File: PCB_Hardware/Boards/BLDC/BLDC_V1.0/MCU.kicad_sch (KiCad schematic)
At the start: 15 parts, among them J7 Conn_ARM_JTAG_SWD_10, U7 STM32G474RET6, Y2 XXGBBCNANF-25.000000MHZ

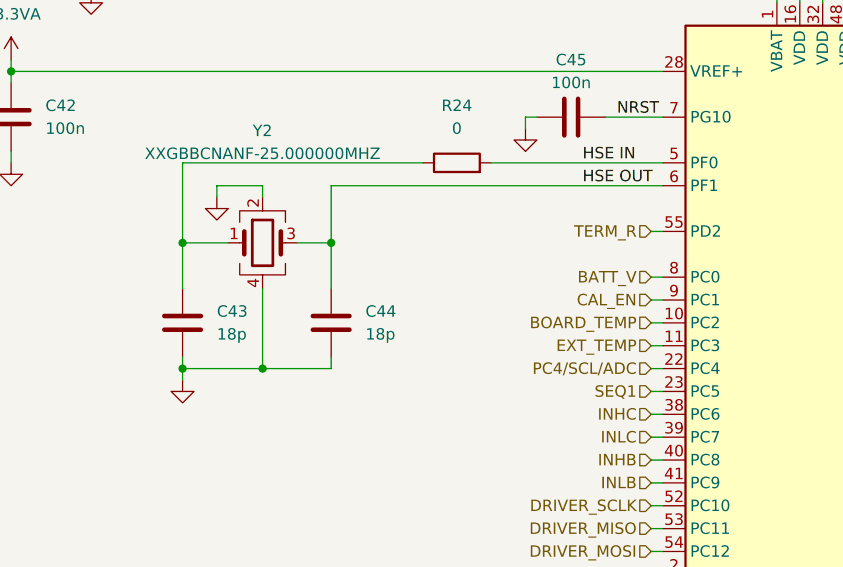
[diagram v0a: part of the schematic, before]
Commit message: Add DBcan transport refactor, BLDC V1.0 schematic + sim work, HAL submodule
- DBcan: replace bare-register driver with vendor-agnostic transport abstraction (core/, transports/, refactored bootloader driver, README)
- Add stm32g4xx_hal_driver as Firmware/libs submodule
- Add HAL config for BLDC board (stm32g4xx_hal_conf.h)
- BLDC V1.0: schematic edits across 10 sheets (footprint assignments, repositioning); design-doc README (gate-driver constraints, FET selection / TPH3R70APL, thermal analysis)
- ngspice simulation workflow (cap sweeps, half-bridge slow turn-on)
- Ignore .obsidian/ vault state and large simulation CSV exports
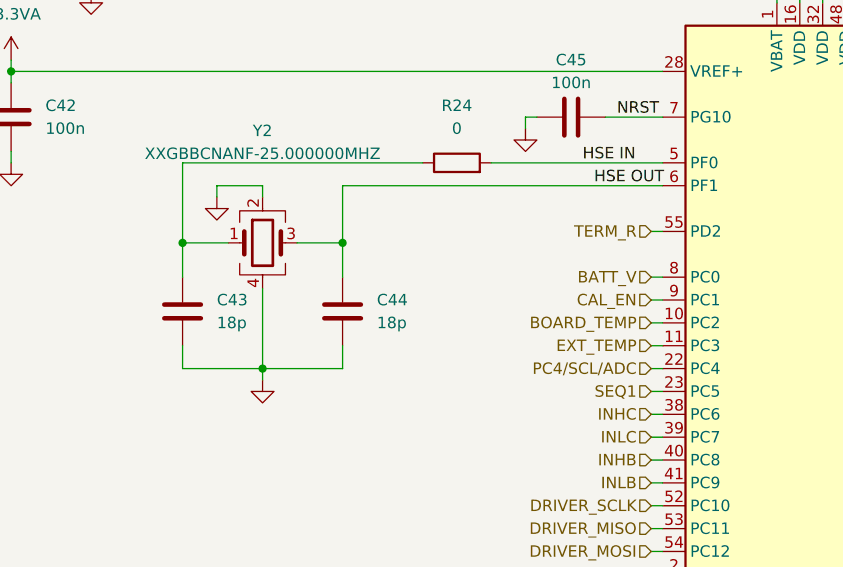
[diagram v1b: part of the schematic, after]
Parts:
- C30: footprint (none) -> Capacitor_SMD:C_0603_1608Metric
- C31, C32, C33, C34, C35, C36, C42, C45: footprint (none) -> Capacitor_SMD:C_0402_1005Metric
- R24: footprint (none) -> Resistor_SMD:R_0402_1005Metric
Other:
- moved on the sheet: C43, C44
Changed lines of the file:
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@@
 	)
 	(junction
-		(at 90.17 76.2)
-		(diameter 0)
-		(color 0 0 0 0)
-	)
-	(junction
 		(at 139.7 36.83)
 		(diameter 0)
@@
 	)
 	(junction
-		(at 73.66 76.2)
-		(diameter 0)
-		(color 0 0 0 0)
-	)
-	(junction
 		(at 88.9 46.99)
 		(diameter 0)
@@
 	)
 	(junction
-		(at 101.6 36.83)
+		(at 73.66 76.2)
 		(diameter 0)
 		(color 0 0 0 0)
 	)
 	(junction
-		(at 73.66 90.17)
+		(at 101.6 36.83)
 		(diameter 0)
 		(color 0 0 0 0)
@@
 	)
 	(junction
+		(at 91.44 76.2)
+		(diameter 0)
+		(color 0 0 0 0)
+	)
+	(junction
 		(at 139.7 48.26)
 		(diameter 0)
@@
 	(wire
 		(pts
-			(xy 82.55 90.17) (xy 90.17 90.17)
+			(xy 82.55 90.17) (xy 91.44 90.17)
 		)
 		(stroke
@@
 	(wire
 		(pts
-			(xy 90.17 69.85) (xy 90.17 76.2)
+			(xy 91.44 69.85) (xy 91.44 76.2)
 		)
 		(stroke
@@
 	(wire
 		(pts
-			(xy 73.66 81.28) (xy 73.66 76.2)
+			(xy 73.66 80.01) (xy 73.66 76.2)
 		)
 		(stroke
@@
 	(wire
 		(pts
-			(xy 73.66 88.9) (xy 73.66 90.17)
+			(xy 73.66 87.63) (xy 73.66 90.17)
 		)
 		(stroke
@@
 	(wire
 		(pts
-			(xy 90.17 81.28) (xy 90.17 76.2)
+			(xy 91.44 80.01) (xy 91.44 76.2)
 		)
 		(stroke
@@
 	(wire
 		(pts
-			(xy 90.17 88.9) (xy 90.17 90.17)
+			(xy 91.44 87.63) (xy 91.44 90.17)
 		)
 		(stroke
@@
 	(wire
 		(pts
-			(xy 127 69.85) (xy 90.17 69.85)
+			(xy 127 69.85) (xy 91.44 69.85)
 		)
 		(stroke
@@
 	(wire
 		(pts
-			(xy 73.66 90.17) (xy 73.66 91.44)
+			(xy 82.55 90.17) (xy 82.55 91.44)
 		)
 		(stroke
@@
 	(wire
 		(pts
-			(xy 86.36 76.2) (xy 90.17 76.2)
+			(xy 86.36 76.2) (xy 91.44 76.2)
 		)
 		(stroke
@@
 	)
 	(label "HSE OUT"
-		(at 118.11 69.85 0)
+		(at 119.38 69.85 0)
 		(effects
 			(font
@@
 	(symbol
 		(lib_id "Device:C")
-		(at 73.66 85.09 0)
+		(at 73.66 83.82 0)
 		(unit 1)
 		(body_style 1)
@@
 		(dnp no)
 		(property "Reference" "C43"
-			(at 77.47 83.8199 0)
+			(at 77.47 82.5499 0)
 			(show_name no)
 			(do_not_autoplace no)
@@
 		)
 		(property "Value" "18p"
-			(at 77.47 86.3599 0)
+			(at 77.47 85.0899 0)
 			(show_name no)
 			(do_not_autoplace no)
@@
 		)
 		(property "Footprint" "Capacitor_SMD:C_0402_1005Metric"
-			(at 74.6252 88.9 0)
+			(at 74.6252 87.63 0)
 			(hide yes)
 			(show_name no)
@@
 		)
 		(property "Datasheet" ""
-			(at 73.66 85.09 0)
+			(at 73.66 83.82 0)
 			(hide yes)
 			(show_name no)
@@
 		)
 		(property "Description" "Unpolarized capacitor"
-			(at 73.66 85.09 0)
+			(at 73.66 83.82 0)
 			(hide yes)
 			(show_name no)
@@
 		)
 		(property "JLCPCB Part Number" "C52923"
-			(at 73.66 85.09 0)
+			(at 73.66 83.82 0)
 			(hide yes)
 			(show_name no)
@@
 		)
 		(property "Sim.Device" ""
-			(at 73.66 85.09 0)
+			(at 73.66 83.82 0)
 			(hide yes)
 			(show_name no)
@@
 		)
 		(property "Price" ""
-			(at 73.66 85.09 0)
+			(at 73.66 83.82 0)
 			(hide yes)
 			(show_name no)
@@
 			)
 		)
-		(property "Footprint" ""
+		(property "Footprint" "Capacitor_SMD:C_0402_1005Metric"
 			(at 102.5652 45.72 0)
 			(hide yes)
@@
 	(symbol
 		(lib_id "Device:C")
-		(at 90.17 85.09 0)
+		(at 91.44 83.82 0)
 		(unit 1)
 		(body_style 1)
@@
 		(dnp no)
 		(property "Reference" "C44"
-			(at 93.98 83.8199 0)
+			(at 95.25 82.5499 0)
 			(show_name no)
 			(do_not_autoplace no)
@@
 		)
 		(property "Value" "18p"
-			(at 93.98 86.3599 0)
+			(at 95.25 85.0899 0)
 			(show_name no)
 			(do_not_autoplace no)
@@
 		)
 		(property "Footprint" "Capacitor_SMD:C_0402_1005Metric"
-			(at 91.1352 88.9 0)
+			(at 92.4052 87.63 0)
 			(hide yes)
 			(show_name no)
@@
 		)
 		(property "Datasheet" ""
-			(at 90.17 85.09 0)
+			(at 91.44 83.82 0)
 			(hide yes)
 			(show_name no)
@@
 		)
 		(property "Description" "Unpolarized capacitor"
-			(at 90.17 85.09 0)
+			(at 91.44 83.82 0)
 			(hide yes)
 			(show_name no)
@@
 		)
 		(property "JLCPCB Part Number" "C52923"
-			(at 90.17 85.09 0)
+			(at 91.44 83.82 0)
 			(hide yes)
 			(show_name no)
@@
 		)
 		(property "Sim.Device" ""
-			(at 90.17 85.09 0)
+			(at 91.44 83.82 0)
 			(hide yes)
 			(show_name no)
@@
 		)
 		(property "Price" ""
-			(at 90.17 85.09 0)
+			(at 91.44 83.82 0)
 			(hide yes)
 			(show_name no)
@@
 			)
 		)
-		(property "Footprint" ""
+		(property "Footprint" "Capacitor_SMD:C_0402_1005Metric"
 			(at 158.4452 46.99 0)
 			(hide yes)
@@
 			)
 		)
-		(property "Footprint" ""
+		(property "Footprint" "Capacitor_SMD:C_0402_1005Metric"
 			(at 89.8652 45.72 0)
 			(hide yes)
@@
 			)
 		)
-		(property "Footprint" ""
+		(property "Footprint" "Capacitor_SMD:C_0402_1005Metric"
 			(at 115.2652 45.72 0)
 			(hide yes)
@@
 	(symbol
 		(lib_id "power:GND")
-		(at 73.66 91.44 0)
+		(at 82.55 91.44 0)
 		(unit 1)
 		(body_style 1)
@@
 		(fields_autoplaced yes)
 		(property "Reference" "#PWR050"
-			(at 73.66 97.79 0)
+			(at 82.55 97.79 0)
 			(hide yes)
 			(show_name no)
@@
 		)
 		(property "Value" "GND"
-			(at 73.66 96.52 0)
+			(at 82.55 96.52 0)
 			(hide yes)
 			(show_name no)
@@
 		)
 		(property "Footprint" ""
-			(at 73.66 91.44 0)
+			(at 82.55 91.44 0)
 			(hide yes)
 			(show_name no)
@@
 		)
 		(property "Datasheet" ""
-			(at 73.66 91.44 0)
+			(at 82.55 91.44 0)
 			(hide yes)
 			(show_name no)
@@
 		)
 		(property "Description" "Power symbol creates a global label with name \"GND\" , ground"
-			(at 73.66 91.44 0)
+			(at 82.55 91.44 0)
 			(hide yes)
 			(show_name no)
@@
 			)
 		)
-		(property "Footprint" ""
+		(property "Footprint" "Capacitor_SMD:C_0402_1005Metric"
 			(at 127.9652 45.72 0)
 			(hide yes)
@@
 			)
 		)
-		(property "Footprint" ""
+		(property "Footprint" "Capacitor_SMD:C_0402_1005Metric"
 			(at 55.5752 66.04 0)
 			(hide yes)
@@
 			)
 		)
-		(property "Footprint" ""
+		(property "Footprint" "Capacitor_SMD:C_0603_1608Metric"
 			(at 64.4652 45.72 0)
 			(hide yes)
@@
 			)
 		)
-		(property "Footprint" ""
+		(property "Footprint" "Capacitor_SMD:C_0402_1005Metric"
 			(at 120.65 61.2648 0)
 			(hide yes)
@@
 			)
 		)
-		(property "Footprint" ""
+		(property "Footprint" "Capacitor_SMD:C_0402_1005Metric"
 			(at 77.1652 45.72 0)
 			(hide yes)
@@
 			)
 		)
-		(property "Footprint" ""
+		(property "Footprint" "Resistor_SMD:R_0402_1005Metric"
 			(at 104.14 69.088 90)
 			(hide yes)

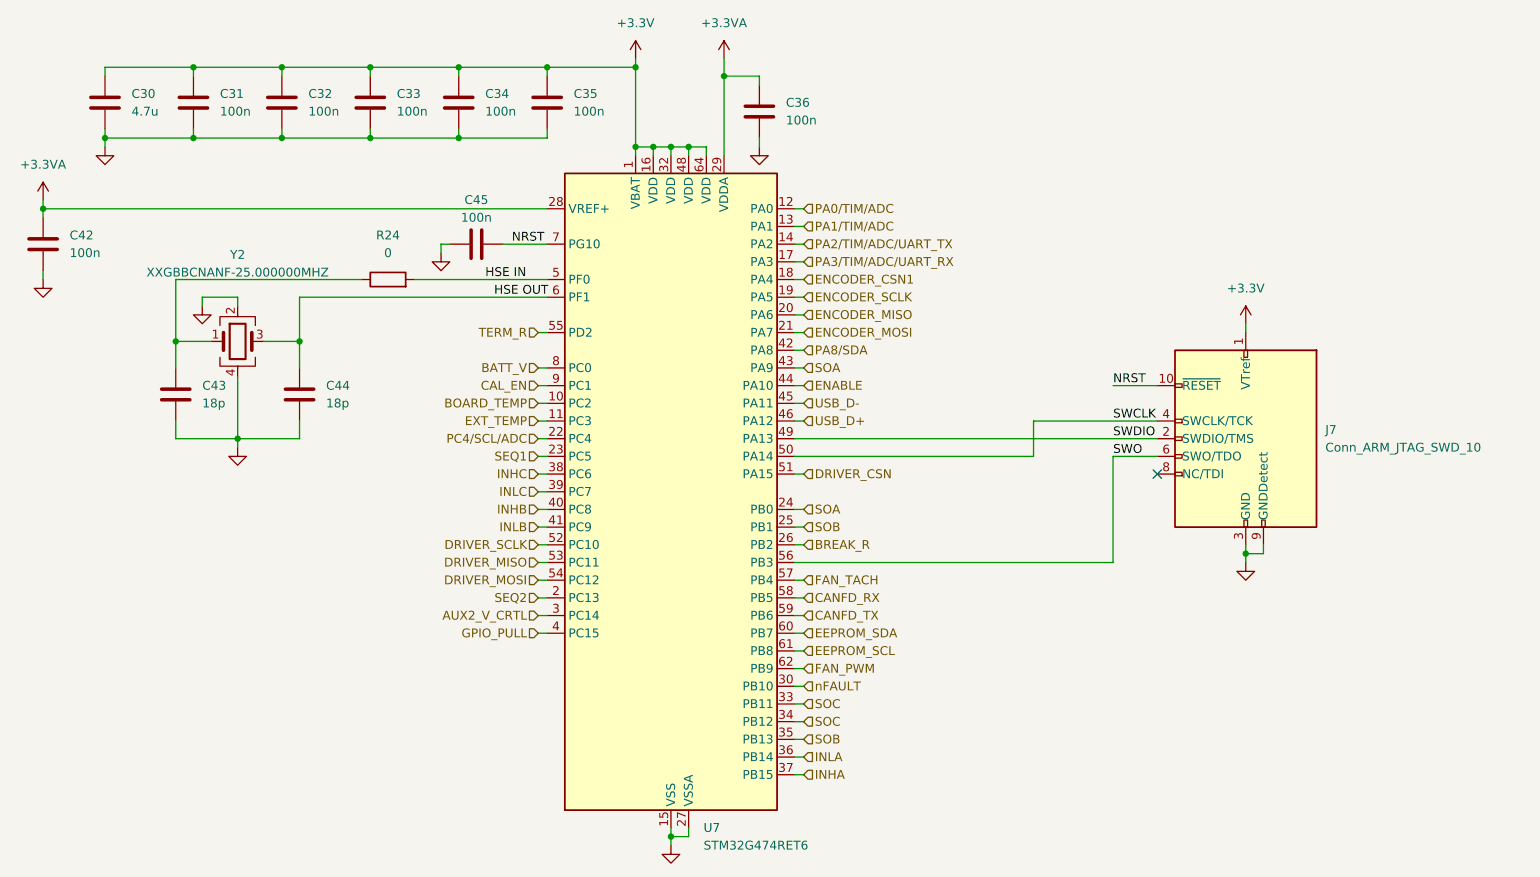
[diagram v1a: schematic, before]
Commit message: Created organization around the symbol lib and did a first pass layout of the BDLC
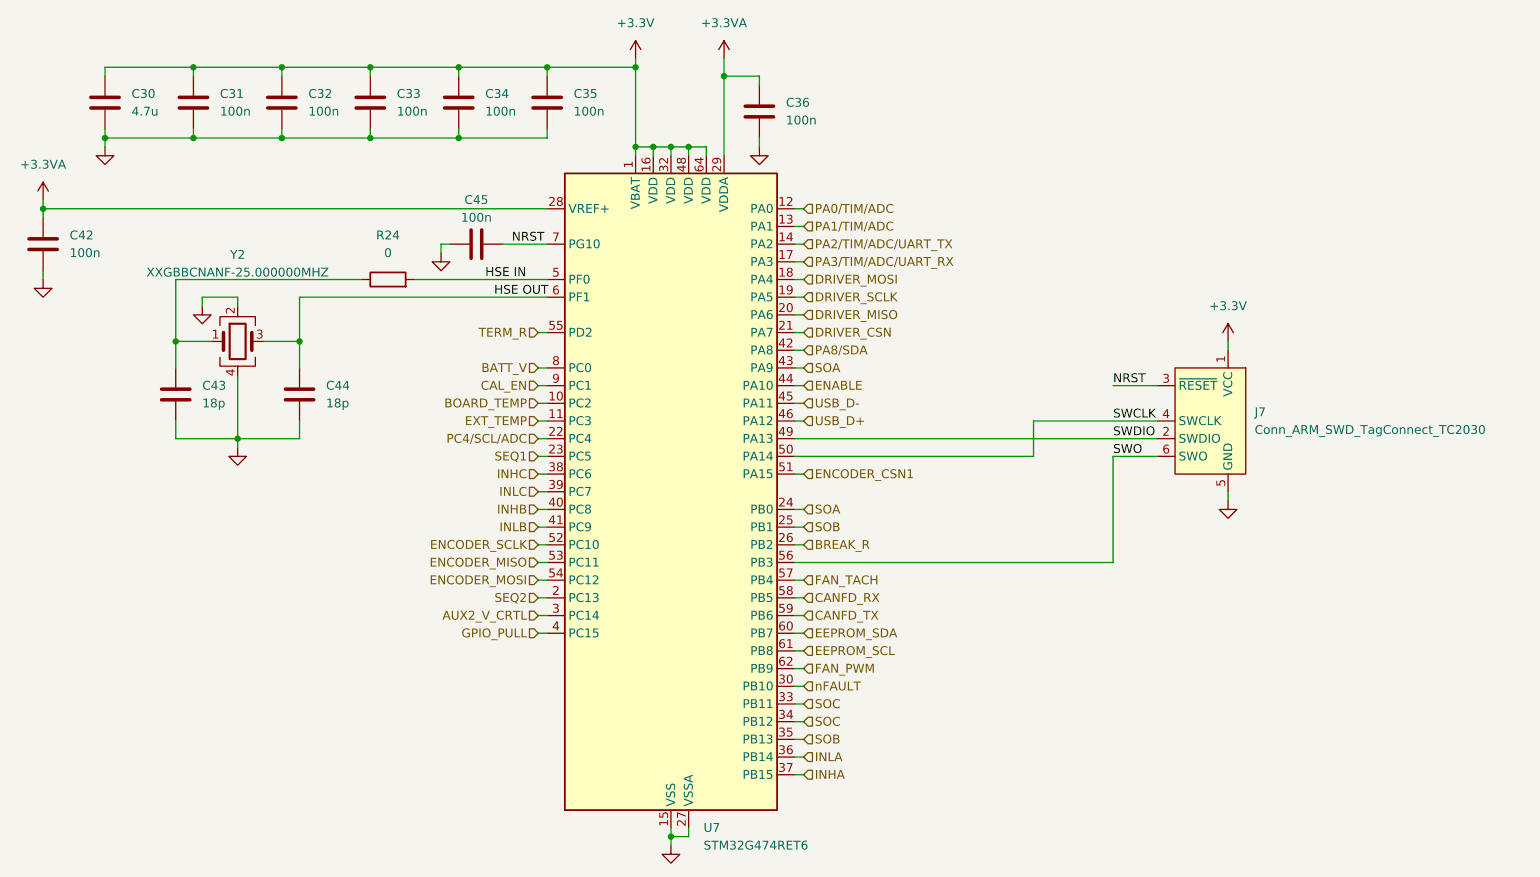
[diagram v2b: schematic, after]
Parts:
- removed J7: Conn_ARM_JTAG_SWD_10, Connector_PinHeader_1.27mm:PinHeader_2x05_P1.27mm_Vertical, symbol Connector:Conn_ARM_JTAG_SWD_10
- added J7: Conn_ARM_SWD_TagConnect_TC2030, Connector:Tag-Connect_TC2030-IDC-FP_2x03_P1.27mm_Vertical, symbol Connector:Conn_ARM_SWD_TagConnect_TC2030
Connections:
- net +3.3V: now also J7.1 (VCC)
- net DRIVER_CSN: now also U7.21 (PA7); no longer U7.51 (PA15)
- net DRIVER_MISO: now also U7.20 (PA6); no longer U7.53 (PC11)
- net DRIVER_MOSI: now also U7.18 (PA4); no longer U7.54 (PC12)
- net DRIVER_SCLK: now also U7.19 (PA5); no longer U7.52 (PC10)
- net ENCODER_CSN1: now also U7.51 (PA15); no longer U7.18 (PA4)
- net ENCODER_MISO: now also U7.53 (PC11); no longer U7.20 (PA6)
- net ENCODER_MOSI: now also U7.54 (PC12); no longer U7.21 (PA7)
- net ENCODER_SCLK: now also U7.52 (PC10); no longer U7.19 (PA5)
- net GND: now also J7.5 (GND)
- net NRST: now also J7.3 (~{RESET})
- net SWCLK: now also J7.4 (SWCLK)
- net SWDIO: now also J7.2 (SWDIO)
- net SWO: now also J7.6 (SWO)
- no-connect marks 1 -> 0

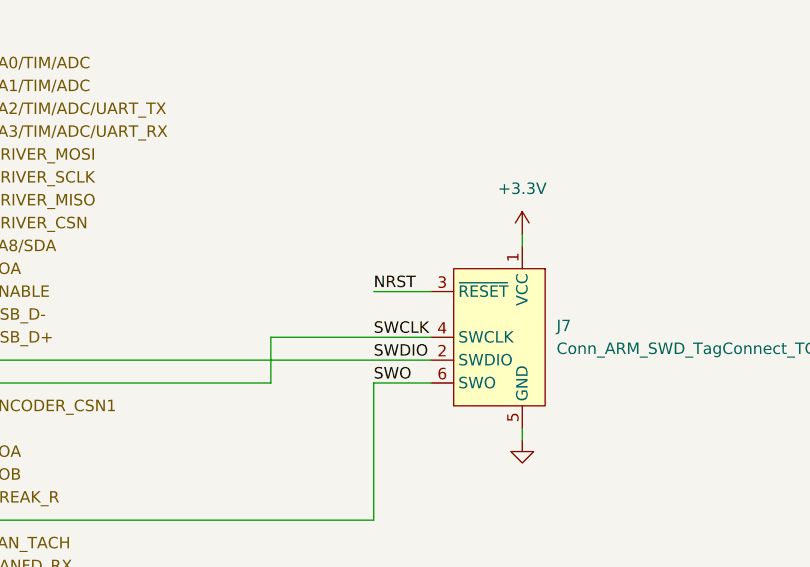
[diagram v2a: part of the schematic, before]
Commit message: complete redo of the BLDC layout
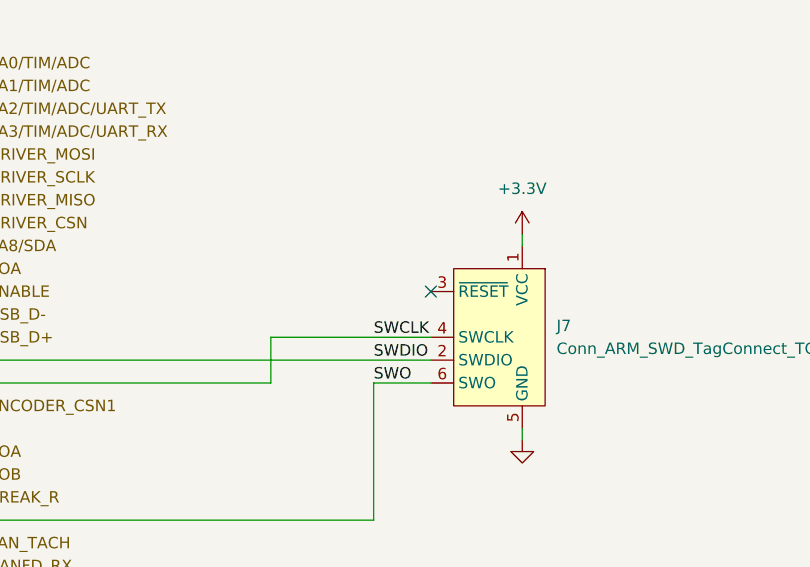
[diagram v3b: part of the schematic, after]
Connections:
- net NRST: no longer J7.3 (~{RESET})
- no-connect marks 0 -> 1
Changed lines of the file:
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@@
 		(color 0 0 0 0)
 	)
+	(no_connect
+		(at 214.63 82.55)
+	)
 	(wire
 		(pts
@@
 		(pts
 			(xy 120.65 62.23) (xy 127 62.23)
-		)
-		(stroke
-			(width 0)
-			(type default)
-		)
-	)
-	(wire
-		(pts
-			(xy 208.28 82.55) (xy 214.63 82.55)
 		)
 		(stroke
@@
 		(effects
 			(font
-				(size 1.27 1.27)
-			)
-			(justify left bottom)
-		)
-	)
-	(label "NRST"
-		(at 208.28 82.55 0)
-		(effects
-			(font
